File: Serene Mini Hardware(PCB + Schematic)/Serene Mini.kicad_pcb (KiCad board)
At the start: 6 copper layers, 25 x 42.5 mm, 81 parts, among them J1 Conn_Coaxial, J2 Conn_01x06_Socket, J4 AudioJack3_Switch, J5 USB_C_Receptacle_USB2.0_14P, J6 Conn_Coaxial, T1 Transformer_1P_1S, U1 AP7361C-33E, U2 AP2112K-1.8, U3 STM32H753ZITx, U4 ADXL382-1BCCZ-RL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

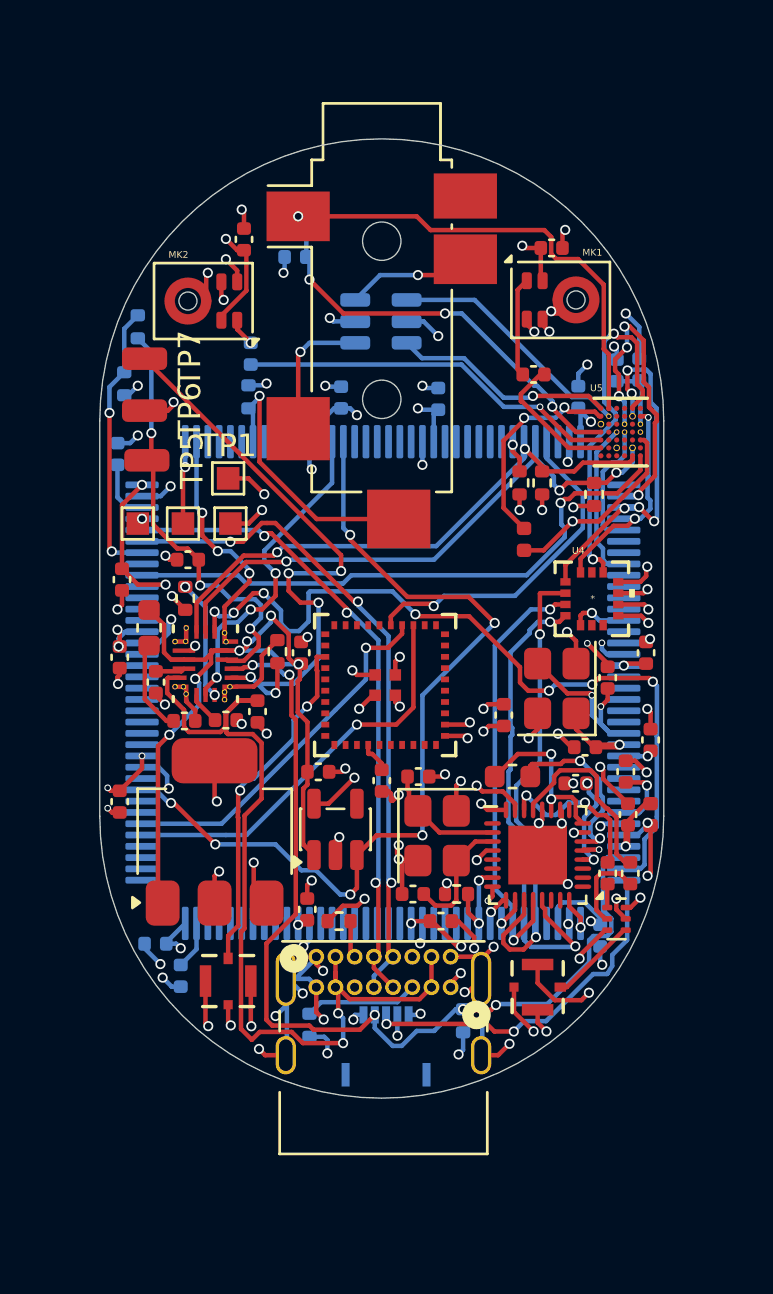
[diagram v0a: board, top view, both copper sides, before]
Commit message: Added Stitching Vias
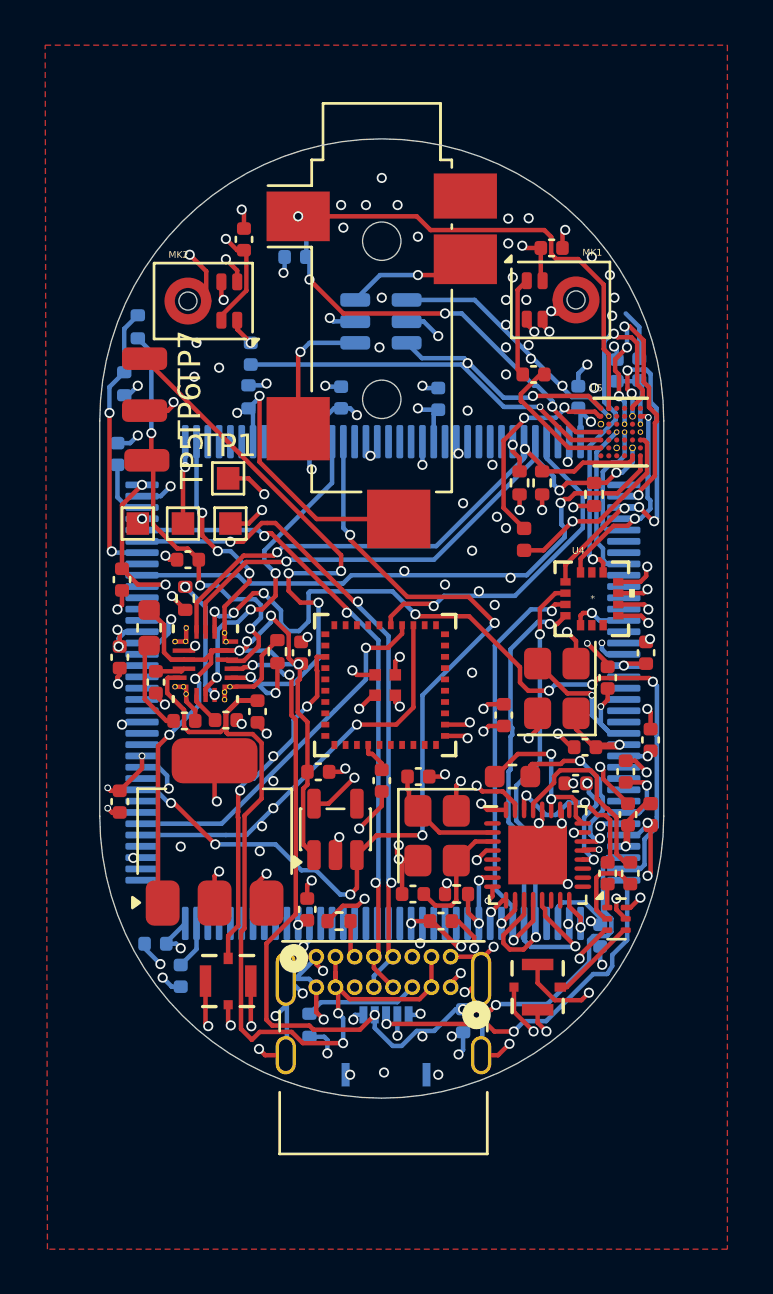
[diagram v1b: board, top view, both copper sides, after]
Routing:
- net GND: track 120.2 -> 122.1 mm, vias 98 -> 154
- added copper zone on F.Cu, net GND

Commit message: Changes to PCB
- Added 2 more filled zones, 1 on layer 3 and 4 respectively

- Added stitching vias

- Fixed some DRC Issues
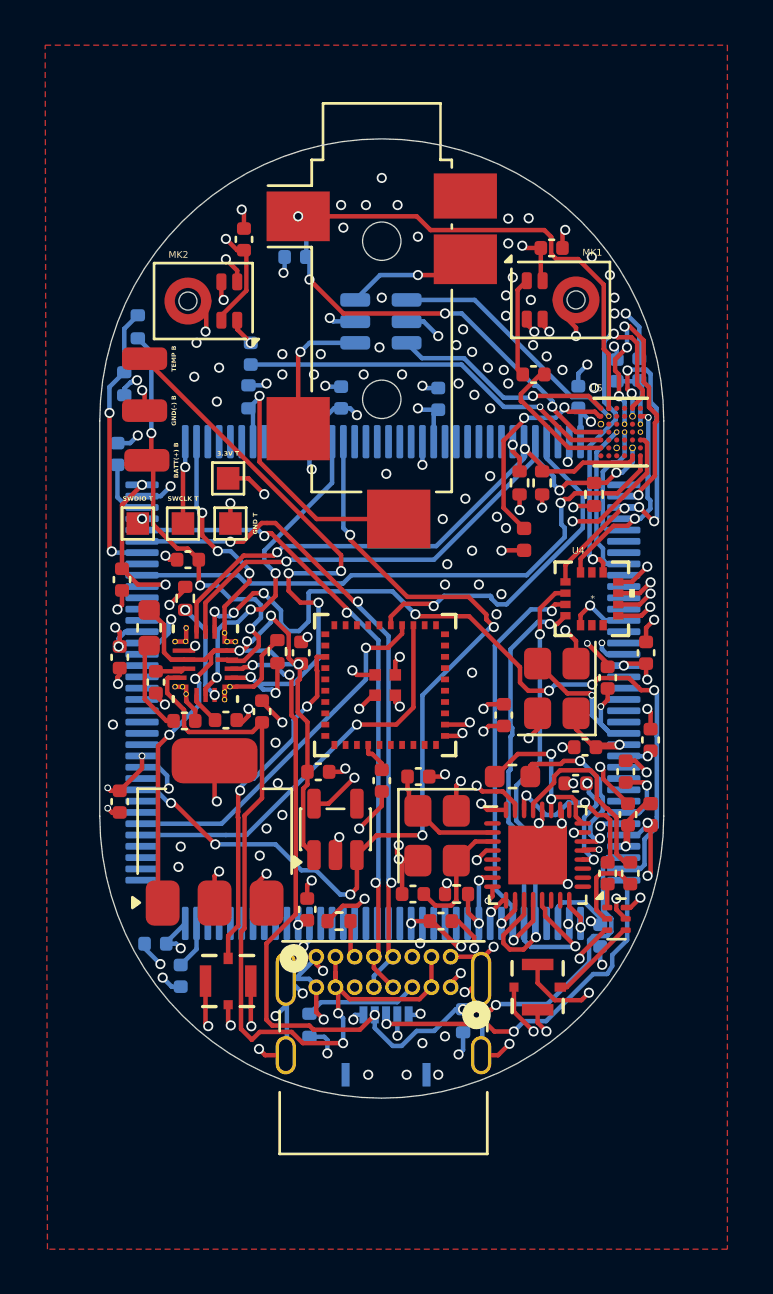
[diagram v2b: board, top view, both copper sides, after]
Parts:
- 3.3V T: renamed from TP1
- moved C40 0.20 mm to (27.9, 61.6), turned to -90 degrees
- turned R6 to 90 degrees
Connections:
- U6 pad 1: Net-(U6-BTST) -> GND
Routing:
- net /VBUS: track 40.0 -> 36.2 mm
- net +1V8: track 50.3 -> 53.5 mm, vias 5 -> 6
- net GND: track 122.1 -> 123.8 mm, vias 154 -> 166
- net Net-(U6-ILIM): track 5.33 -> 4.31 mm
- net /V_SYS: track 35.5 -> 34.8 mm
- net +3.3V: track 55.9 -> 56.2 mm, vias 35 -> 36
- added copper zone on In2.Cu, net GND
- added copper zone on In3.Cu, net GND
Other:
- board text added: "BATT(+) B"
- board text added: "GND T"
- board text added: "GND(-) B"
- board text added: "SWCLK T"
- board text added: "SWDIO T"
- board text added: "TEMP B"

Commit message: Fixed Issues with PCB
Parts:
- TP1: renamed from 3.3V T
- moved TP3 0.10 mm to (26.4, 53.3)
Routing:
- net +3.3V: track 56.2 -> 60.8 mm
- net GND: vias 166 -> 167
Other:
- board text added: "3.3V T"
